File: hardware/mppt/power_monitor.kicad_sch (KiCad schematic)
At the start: 16 parts, among them IC701 INA229AIDGSR

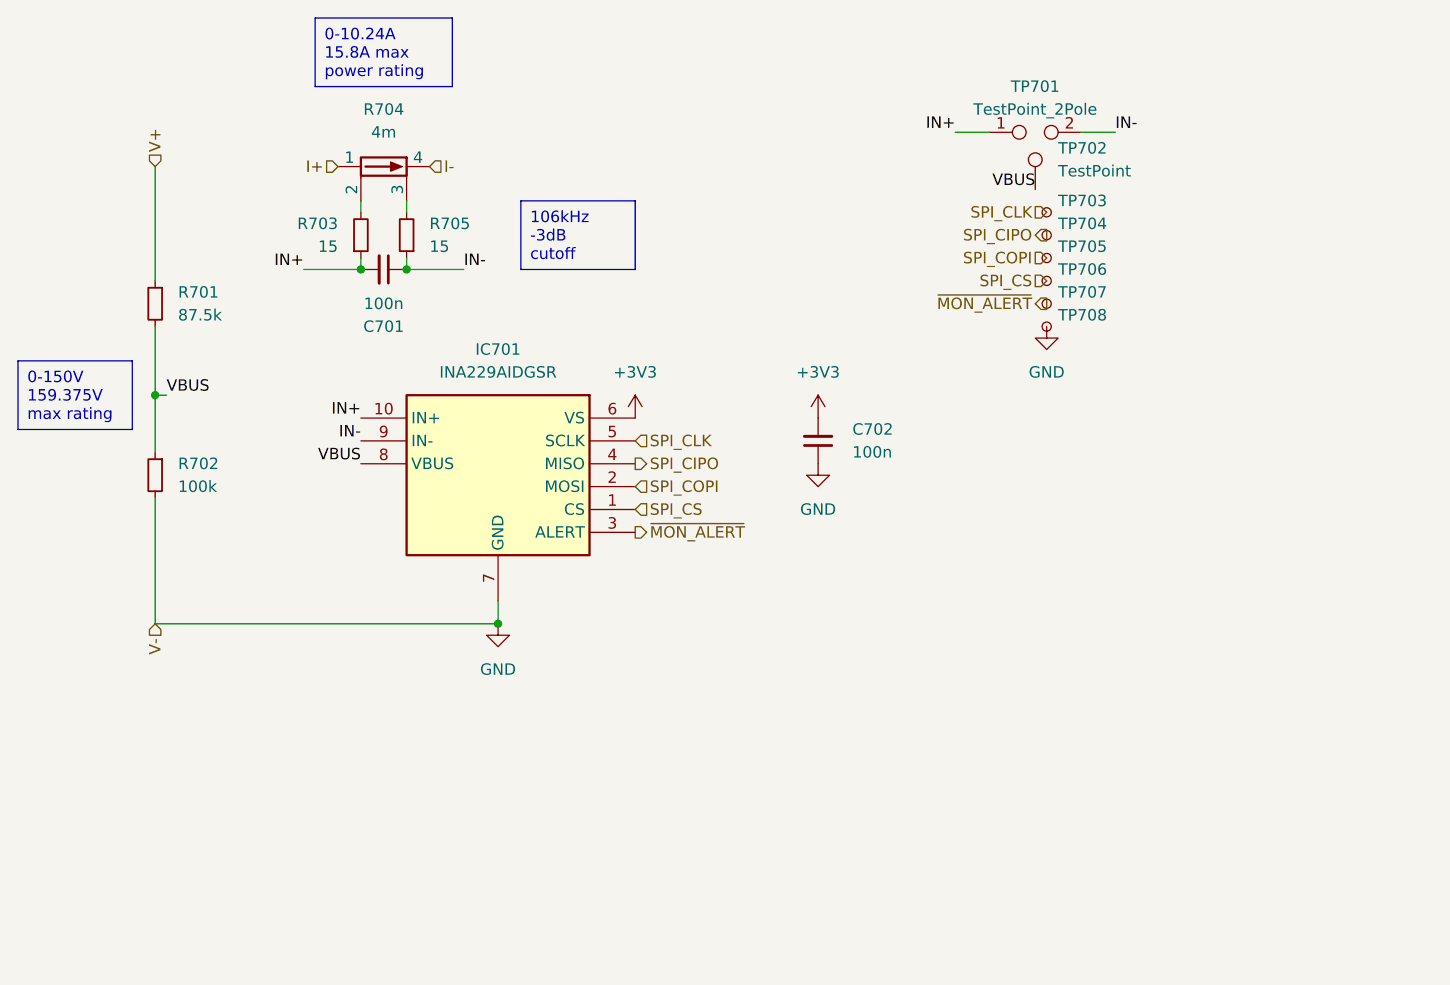
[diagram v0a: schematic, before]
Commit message: run through mppt sch, going through bom
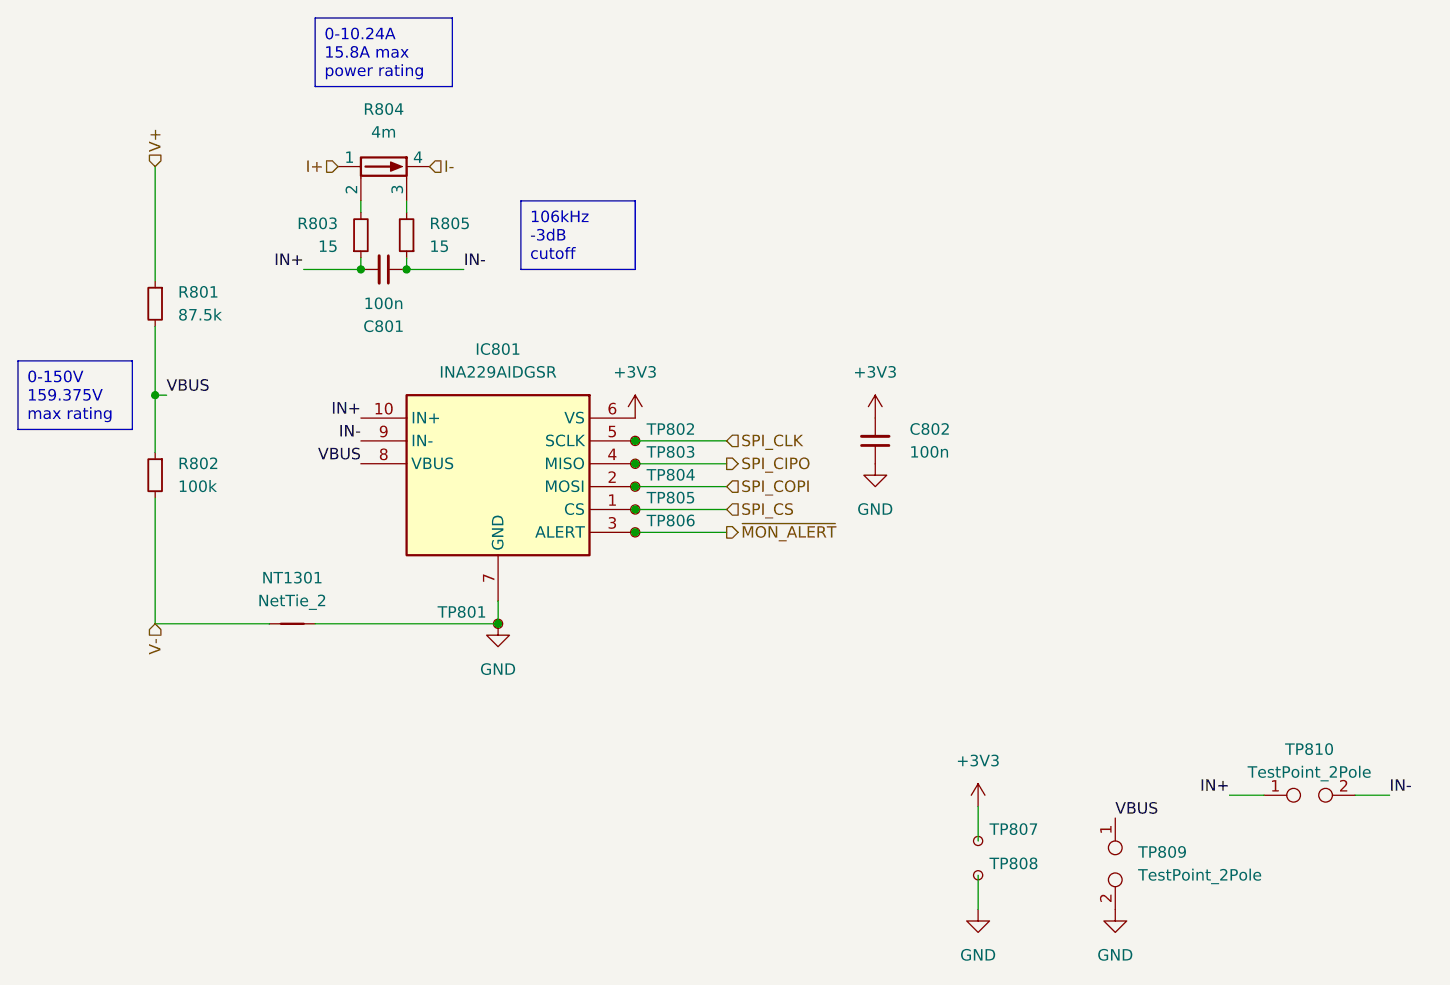
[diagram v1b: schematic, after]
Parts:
- removed TP702: TestPoint, TestPoint:TestPoint_Keystone_5000-5004_Miniature, symbol Connector:TestPoint
- removed TP703, TP704, TP705, TP706, TP707, TP708: TestPoint_Small, TestPoint:TestPoint_Keystone_5000-5004_Miniature, symbol Connector:TestPoint_Small
- added NT1301: NetTie_2, symbol Device:NetTie_2
- added TP801, TP802, TP803, TP804, TP805, TP806: TestPoint_Small, TestPoint:TestPoint_Keystone_5000-5004_Miniature, symbol Connector:TestPoint_Small
- added TP807, TP808: TestPoint_Small, TestPoint:TestPoint_Pad_D1.0mm, symbol Connector:TestPoint_Small
- added TP809: TestPoint_2Pole, symbol Connector:TestPoint_2Pole
- C801: renamed from C701; footprint Capacitor_SMD:C_0805_2012Metric_Pad1.18x1.45mm_HandSolder -> (none); Manufacturer Samsung Microelectronics -> Samsung Electro-Mechanics
- C802: renamed from C702; footprint Capacitor_SMD:C_0805_2012Metric_Pad1.18x1.45mm_HandSolder -> (none); Manufacturer Samsung Microelectronics -> Samsung Electro-Mechanics; Notes 3.3V -> 3.3V Rating
- IC801: renamed from IC701; Distributor Texas Instruments -> (none)
- renumbered R701 to R801, R702 to R802, R703 to R803, R704 to R804, R705 to R805, TP701 to TP810
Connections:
- net +3V3: now also TP807.1
- net GND: now also NT1301.2, TP801.1, TP808.1, TP809.2; no longer R802.2
- net SPI_CIPO: now also TP803.1
- net SPI_CLK: now also TP802.1
- net SPI_COPI: now also TP804.1
- net SPI_CS: now also TP805.1
- net VBUS: now also TP809.1
- net ~{MON_ALERT}: now also TP806.1
- new net V-: NT1301.1, R802.2
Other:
- moved on the sheet: C802, TP810

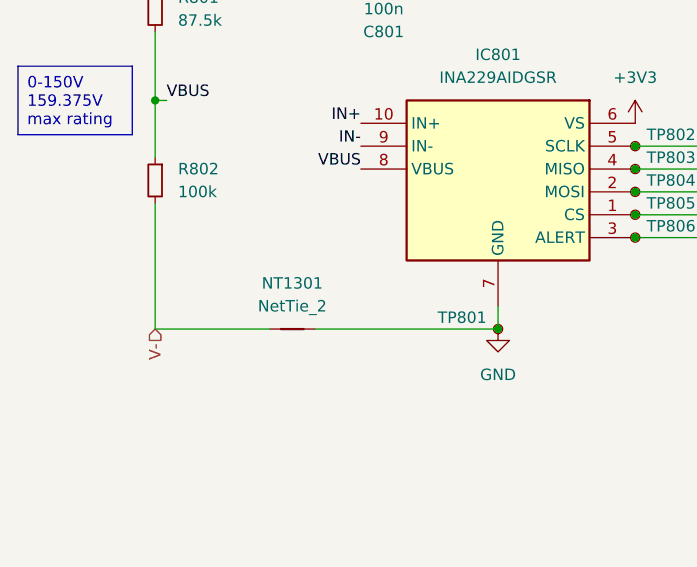
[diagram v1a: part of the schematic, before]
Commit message: update final missing pieces for sch, moving to bom pop
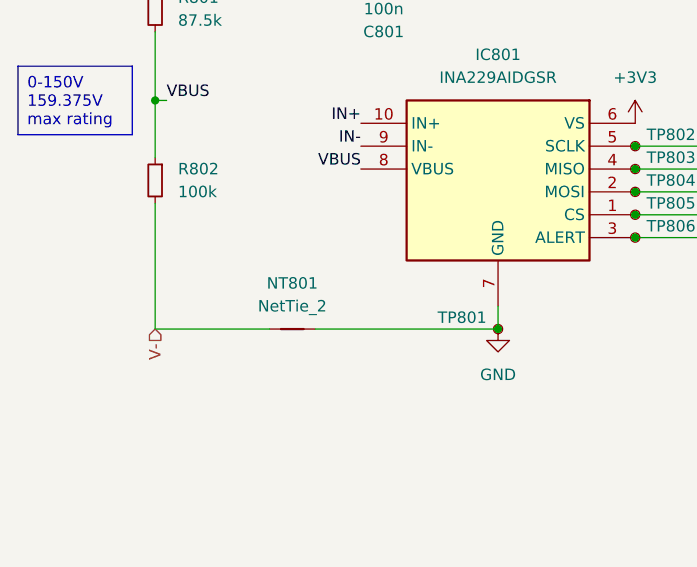
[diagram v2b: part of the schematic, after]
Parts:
- NT801: renamed from NT1301; footprint (none) -> NetTie:NetTie-2_SMD_Pad2.0mm
- R801, R802, R803, R805: footprint Resistor_SMD:R_0805_2012Metric_Pad1.20x1.40mm_HandSolder -> (none)
- TP801, TP802, TP803, TP804, TP805, TP806: footprint TestPoint:TestPoint_Keystone_5000-5004_Miniature -> TestPoint:TestPoint_Pad_D1.0mm; Manufacturer Keystone Electronics -> (none); P/N 5000 -> (none)
- TP809, TP810: footprint (none) -> TestPoint:TestPoint_2Pads_Pitch2.54mm_Drill0.8mm
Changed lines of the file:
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@@
 			)
 		)
-		(property "Footprint" ""
+		(property "Footprint" "TestPoint:TestPoint_2Pads_Pitch2.54mm_Drill0.8mm"
 			(at 217.17 146.05 0)
 			(effects
@@
 			)
 		)
-		(property "Datasheet" "~"
+		(property "Datasheet" ""
 			(at 217.17 146.05 0)
 			(effects
@@
 			)
 		)
-		(property "Footprint" "Resistor_SMD:R_0805_2012Metric_Pad1.20x1.40mm_HandSolder"
+		(property "Footprint" ""
 			(at 88.9 110.49 0)
 			(effects
@@
 			)
 		)
-		(property "Footprint" "Resistor_SMD:R_0805_2012Metric_Pad1.20x1.40mm_HandSolder"
+		(property "Footprint" ""
 			(at 116.84 83.82 0)
 			(effects
@@
 			)
 		)
-		(property "Footprint" "TestPoint:TestPoint_Keystone_5000-5004_Miniature"
+		(property "Footprint" "TestPoint:TestPoint_Pad_D1.0mm"
 			(at 147.32 114.3 0)
 			(effects
@@
 			)
 		)
-		(property "Datasheet" "https://www.keyelco.com/userAssets/file/M65p56.pdf"
+		(property "Datasheet" ""
 			(at 147.32 114.3 0)
 			(effects
@@
 			)
 		)
-		(property "Manufacturer" "Keystone Electronics"
+		(property "Manufacturer" ""
 			(at 142.24 114.3 0)
 			(effects
@@
 			)
 		)
-		(property "P/N" "5000"
+		(property "P/N" ""
 			(at 142.24 114.3 0)
 			(effects
@@
 			)
 		)
-		(property "Footprint" "Resistor_SMD:R_0805_2012Metric_Pad1.20x1.40mm_HandSolder"
+		(property "Footprint" ""
 			(at 111.76 83.82 0)
 			(effects
@@
 			)
 		)
-		(property "Footprint" "Resistor_SMD:R_0805_2012Metric_Pad1.20x1.40mm_HandSolder"
+		(property "Footprint" ""
 			(at 88.9 91.44 0)
 			(effects
@@
 			)
 		)
-		(property "Footprint" "TestPoint:TestPoint_Keystone_5000-5004_Miniature"
+		(property "Footprint" "TestPoint:TestPoint_Pad_D1.0mm"
 			(at 147.32 109.22 0)
 			(effects
@@
 			)
 		)
-		(property "Datasheet" "https://www.keyelco.com/userAssets/file/M65p56.pdf"
+		(property "Datasheet" ""
 			(at 147.32 109.22 0)
 			(effects
@@
 			)
 		)
-		(property "Manufacturer" "Keystone Electronics"
+		(property "Manufacturer" ""
 			(at 142.24 109.22 0)
 			(effects
@@
 			)
 		)
-		(property "P/N" "5000"
+		(property "P/N" ""
 			(at 142.24 109.22 0)
 			(effects
@@
 			)
 		)
-		(property "Footprint" "TestPoint:TestPoint_Keystone_5000-5004_Miniature"
+		(property "Footprint" "TestPoint:TestPoint_Pad_D1.0mm"
 			(at 147.32 116.84 0)
 			(effects
@@
 			)
 		)
-		(property "Datasheet" "https://www.keyelco.com/userAssets/file/M65p56.pdf"
+		(property "Datasheet" ""
 			(at 147.32 116.84 0)
 			(effects
@@
 			)
 		)
-		(property "Manufacturer" "Keystone Electronics"
+		(property "Manufacturer" ""
 			(at 142.24 116.84 0)
 			(effects
@@
 			)
 		)
-		(property "P/N" "5000"
+		(property "P/N" ""
 			(at 142.24 116.84 0)
 			(effects
@@
 			)
 		)
-		(property "Footprint" "TestPoint:TestPoint_Keystone_5000-5004_Miniature"
+		(property "Footprint" "TestPoint:TestPoint_Pad_D1.0mm"
 			(at 147.32 106.68 0)
 			(effects
@@
 			)
 		)
-		(property "Datasheet" "https://www.keyelco.com/userAssets/file/M65p56.pdf"
+		(property "Datasheet" ""
 			(at 147.32 106.68 0)
 			(effects
@@
 			)
 		)
-		(property "Manufacturer" "Keystone Electronics"
+		(property "Manufacturer" ""
 			(at 142.24 106.68 0)
 			(effects
@@
 			)
 		)
-		(property "P/N" "5000"
+		(property "P/N" ""
 			(at 142.24 106.68 0)
 			(effects
@@
 			)
 		)
-		(property "Footprint" "TestPoint:TestPoint_Keystone_5000-5004_Miniature"
+		(property "Footprint" "TestPoint:TestPoint_Pad_D1.0mm"
 			(at 121.92 127 0)
 			(effects
@@
 			)
 		)
-		(property "Datasheet" "https://www.keyelco.com/userAssets/file/M65p56.pdf"
+		(property "Datasheet" ""
 			(at 121.92 127 0)
 			(effects
@@
 			)
 		)
-		(property "Manufacturer" "Keystone Electronics"
+		(property "Manufacturer" ""
 			(at 127 127 0)
 			(effects
@@
 			)
 		)
-		(property "P/N" "5000"
+		(property "P/N" ""
 			(at 127 127 0)
 			(effects
@@
 			)
 		)
-		(property "Footprint" "TestPoint:TestPoint_Keystone_5000-5004_Miniature"
+		(property "Footprint" "TestPoint:TestPoint_Pad_D1.0mm"
 			(at 147.32 111.76 0)
 			(effects
@@
 			)
 		)
-		(property "Datasheet" "https://www.keyelco.com/userAssets/file/M65p56.pdf"
+		(property "Datasheet" ""
 			(at 147.32 111.76 0)
 			(effects
@@
 			)
 		)
-		(property "Manufacturer" "Keystone Electronics"
+		(property "Manufacturer" ""
 			(at 142.24 111.76 0)
 			(effects
@@
 			)
 		)
-		(property "P/N" "5000"
+		(property "P/N" ""
 			(at 142.24 111.76 0)
 			(effects
@@
 		(dnp no)
 		(fields_autoplaced yes)
-		(property "Reference" "NT1301"
+		(property "Reference" "NT801"
 			(at 104.14 121.92 0)
 			(effects
@@
 			)
 		)
-		(property "Footprint" ""
+		(property "Footprint" "NetTie:NetTie-2_SMD_Pad2.0mm"
 			(at 104.14 127 0)
 			(effects
@@
 			)
 		)
-		(property "Datasheet" "~"
+		(property "Datasheet" ""
 			(at 104.14 127 0)
 			(effects
@@
 			)
 		)
-		(property "Footprint" ""
+		(property "Footprint" "TestPoint:TestPoint_2Pads_Pitch2.54mm_Drill0.8mm"
 			(at 195.58 153.67 0)
 			(effects
@@
 			)
 		)
-		(property "Datasheet" "~"
+		(property "Datasheet" ""
 			(at 195.58 153.67 0)
 			(effects

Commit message: bom consolidated, starting layout
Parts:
- C801, C802: footprint (none) -> Capacitor_SMD:C_0402_1005Metric_Pad0.74x0.62mm_HandSolder; Manufacturer Samsung Electro-Mechanics -> TDK; P/N (none) -> CGA2B3X7R1H104K050BB
- NT801: footprint NetTie:NetTie-2_SMD_Pad2.0mm -> NetTie:NetTie-2_SMD_Pad0.5mm
- R801: value 87.5k -> 86.6k; footprint (none) -> Resistor_SMD:R_0603_1608Metric_Pad0.98x0.95mm_HandSolder; P/N (none) -> CRCW060386K6FKEA
- R802: footprint (none) -> Resistor_SMD:R_0603_1608Metric_Pad0.98x0.95mm_HandSolder; P/N (none) -> CRCW0603100KFKEA
- R803, R805: footprint (none) -> Resistor_SMD:R_0603_1608Metric_Pad0.98x0.95mm_HandSolder; P/N (none) -> CRCW060315R0FKEA

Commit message: progress on layout
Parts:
- removed TP801: TestPoint_Small, TestPoint:TestPoint_Pad_D1.0mm, symbol Connector:TestPoint_Small
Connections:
- net GND: no longer TP809.2
- net V-: now also TP809.2
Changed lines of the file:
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@@
+		)
+	)
+	(hierarchical_label "V-"
+		(shape input)
+		(at 195.58 158.75 270)
+		(fields_autoplaced yes)
+		(effects
+			(font
+				(size 1.27 1.27)
+			)
+			(justify right)
 		)
 	)
@@
 				)
 				(path "/83ad0d2f-976b-4ec4-beba-98e6b6988069/1e7e948a-199f-4420-b7b6-1130e9474bfe/ef801f28-5df3-4a7f-a59d-9cf49d40d7d5"
-					(reference "TP1310")
+					(reference "TP1309")
 					(unit 1)
 				)
@@
 				)
 				(path "/83ad0d2f-976b-4ec4-beba-98e6b6988069/1e7e948a-199f-4420-b7b6-1130e9474bfe/ef801f28-5df3-4a7f-a59d-9cf49d40d7d5"
-					(reference "TP1305")
+					(reference "TP1304")
 					(unit 1)
 				)
@@
 				)
 				(path "/83ad0d2f-976b-4ec4-beba-98e6b6988069/1e7e948a-199f-4420-b7b6-1130e9474bfe/ef801f28-5df3-4a7f-a59d-9cf49d40d7d5"
-					(reference "TP1303")
+					(reference "TP1302")
 					(unit 1)
 				)
@@
 				)
 				(path "/83ad0d2f-976b-4ec4-beba-98e6b6988069/1e7e948a-199f-4420-b7b6-1130e9474bfe/ef801f28-5df3-4a7f-a59d-9cf49d40d7d5"
-					(reference "TP1307")
-					(unit 1)
-				)
-			)
-		)
-	)
-	(symbol
-		(lib_id "power:GND")
-		(at 195.58 158.75 0)
-		(unit 1)
-		(exclude_from_sim no)
-		(in_bom yes)
-		(on_board yes)
-		(dnp no)
-		(fields_autoplaced yes)
-		(property "Reference" "#PWR0807"
-			(at 195.58 165.1 0)
-			(effects
-				(font
-					(size 1.27 1.27)
-				)
-				(hide yes)
-			)
-		)
-		(property "Value" "GND"
-			(at 195.58 163.83 0)
-			(effects
-				(font
-					(size 1.27 1.27)
-				)
-			)
-		)
-		(property "Footprint" ""
-			(at 195.58 158.75 0)
-			(effects
-				(font
-					(size 1.27 1.27)
-				)
-				(hide yes)
-			)
-		)
-		(property "Datasheet" ""
-			(at 195.58 158.75 0)
-			(effects
-				(font
-					(size 1.27 1.27)
-				)
-				(hide yes)
-			)
-		)
-		(property "Description" "Power symbol creates a global label with name \"GND\" , ground"
-			(at 195.58 158.75 0)
-			(effects
-				(font
-					(size 1.27 1.27)
-				)
-				(hide yes)
-			)
-		)
-		(property "Sim.Device" ""
-			(at 195.58 158.75 0)
-			(effects
-				(font
-					(size 1.27 1.27)
-				)
-				(hide yes)
-			)
-		)
-		(property "Sim.Pins" ""
-			(at 195.58 158.75 0)
-			(effects
-				(font
-					(size 1.27 1.27)
-				)
-				(hide yes)
-			)
-		)
-		(pin "1"
-		)
-		(instances
-			(project "mppt"
-				(path "/83ad0d2f-976b-4ec4-beba-98e6b6988069/1e7e948a-199f-4420-b7b6-1130e9474bfe/6e1b912f-3d04-4fc7-9635-6a40ec8ca7c8"
-					(reference "#PWR0807")
-					(unit 1)
-				)
-				(path "/83ad0d2f-976b-4ec4-beba-98e6b6988069/1e7e948a-199f-4420-b7b6-1130e9474bfe/ef801f28-5df3-4a7f-a59d-9cf49d40d7d5"
-					(reference "#PWR01307")
+					(reference "TP1306")
 					(unit 1)
 				)
@@
 				)
 				(path "/83ad0d2f-976b-4ec4-beba-98e6b6988069/1e7e948a-199f-4420-b7b6-1130e9474bfe/ef801f28-5df3-4a7f-a59d-9cf49d40d7d5"
-					(reference "TP1306")
+					(reference "TP1305")
 					(unit 1)
 				)
@@
 				)
 				(path "/83ad0d2f-976b-4ec4-beba-98e6b6988069/1e7e948a-199f-4420-b7b6-1130e9474bfe/ef801f28-5df3-4a7f-a59d-9cf49d40d7d5"
-					(reference "TP1302")
-					(unit 1)
-				)
-			)
-		)
-	)
-	(symbol
-		(lib_id "Connector:TestPoint_Small")
-		(at 127 127 0)
-		(mirror y)
-		(unit 1)
-		(exclude_from_sim no)
-		(in_bom yes)
-		(on_board yes)
-		(dnp no)
-		(property "Reference" "TP801"
-			(at 125.73 125.7299 0)
-			(effects
-				(font
-					(size 1.27 1.27)
-				)
-				(justify left)
-			)
-		)
-		(property "Value" "TestPoint_Small"
-			(at 125.73 128.2699 0)
-			(effects
-				(font
-					(size 1.27 1.27)
-				)
-				(justify left)
-				(hide yes)
-			)
-		)
-		(property "Footprint" "TestPoint:TestPoint_Pad_D1.0mm"
-			(at 121.92 127 0)
-			(effects
-				(font
-					(size 1.27 1.27)
-				)
-				(hide yes)
-			)
-		)
-		(property "Datasheet" ""
-			(at 121.92 127 0)
-			(effects
-				(font
-					(size 1.27 1.27)
-				)
-				(hide yes)
-			)
-		)
-		(property "Description" "test point"
-			(at 127 127 0)
-			(effects
-				(font
-					(size 1.27 1.27)
-				)
-				(hide yes)
-			)
-		)
-		(property "Manufacturer" ""
-			(at 127 127 0)
-			(effects
-				(font
-					(size 1.27 1.27)
-				)
-				(hide yes)
-			)
-		)
-		(property "P/N" ""
-			(at 127 127 0)
-			(effects
-				(font
-					(size 1.27 1.27)
-				)
-				(hide yes)
-			)
-		)
-		(pin "1"
-		)
-		(instances
-			(project "mppt"
-				(path "/83ad0d2f-976b-4ec4-beba-98e6b6988069/1e7e948a-199f-4420-b7b6-1130e9474bfe/6e1b912f-3d04-4fc7-9635-6a40ec8ca7c8"
-					(reference "TP801")
-					(unit 1)
-				)
-				(path "/83ad0d2f-976b-4ec4-beba-98e6b6988069/1e7e948a-199f-4420-b7b6-1130e9474bfe/ef801f28-5df3-4a7f-a59d-9cf49d40d7d5"
 					(reference "TP1301")
 					(unit 1)
@@
 				)
 				(path "/83ad0d2f-976b-4ec4-beba-98e6b6988069/1e7e948a-199f-4420-b7b6-1130e9474bfe/ef801f28-5df3-4a7f-a59d-9cf49d40d7d5"
-					(reference "TP1304")
+					(reference "TP1303")
 					(unit 1)
 				)
@@
 				)
 				(path "/83ad0d2f-976b-4ec4-beba-98e6b6988069/1e7e948a-199f-4420-b7b6-1130e9474bfe/ef801f28-5df3-4a7f-a59d-9cf49d40d7d5"
-					(reference "TP1308")
+					(reference "TP1307")
 					(unit 1)
 				)
@@
 				)
 				(path "/83ad0d2f-976b-4ec4-beba-98e6b6988069/1e7e948a-199f-4420-b7b6-1130e9474bfe/ef801f28-5df3-4a7f-a59d-9cf49d40d7d5"
-					(reference "TP1309")
-					(unit 1)
-				)
+					(reference "TP1308")
+					(unit 1)
+				)
